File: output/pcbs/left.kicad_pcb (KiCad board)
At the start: 2 copper layers, 123.1 x 95.2 mm, 45 parts

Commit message: Position JST more robustly
also tuck thumbs up a little more
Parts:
- removed S19, S20, S21, S22, S23, S24, S25, S26, S27, S28, S29, S30, S31, S32, S33, S34, S35, S36: , ceoloide:switch_choc_v1_v2
- moved JST1 5.34 mm to (3.15, 18.9)
- moved H5 2.00 mm to (98.6, 1.56)
- moved S16 2.00 mm to (57.1, 7.18)
- moved S17 2.00 mm to (77.1, 9.48)
- moved S18 2.00 mm to (95.9, 16.3)
- moved H3 1.41 mm to (-5.60, 13.7)
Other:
- board size 123.1 x 95.2 mm -> 123.1 x 93.2 mm

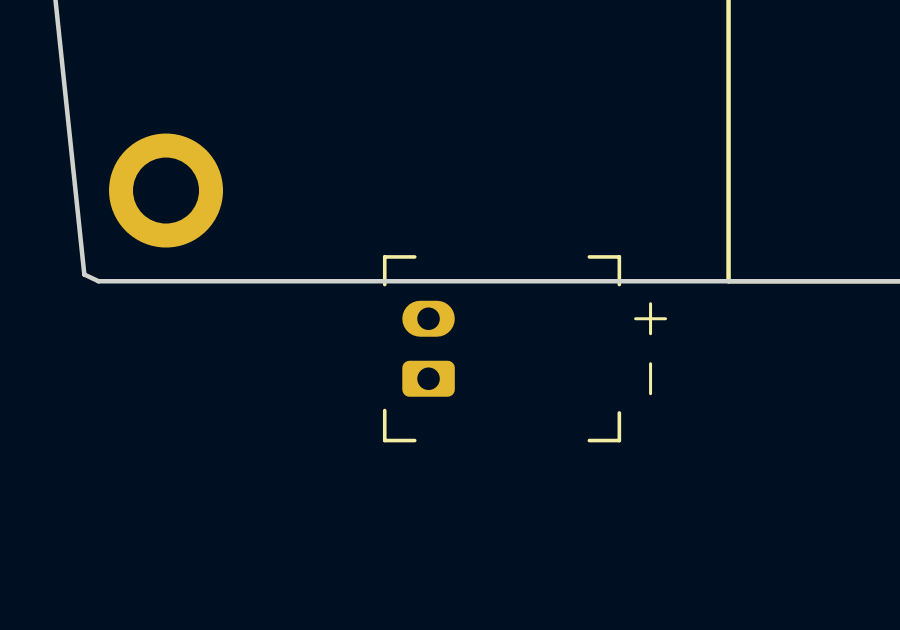
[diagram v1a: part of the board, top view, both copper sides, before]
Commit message: Make jst pcb and outline behave better
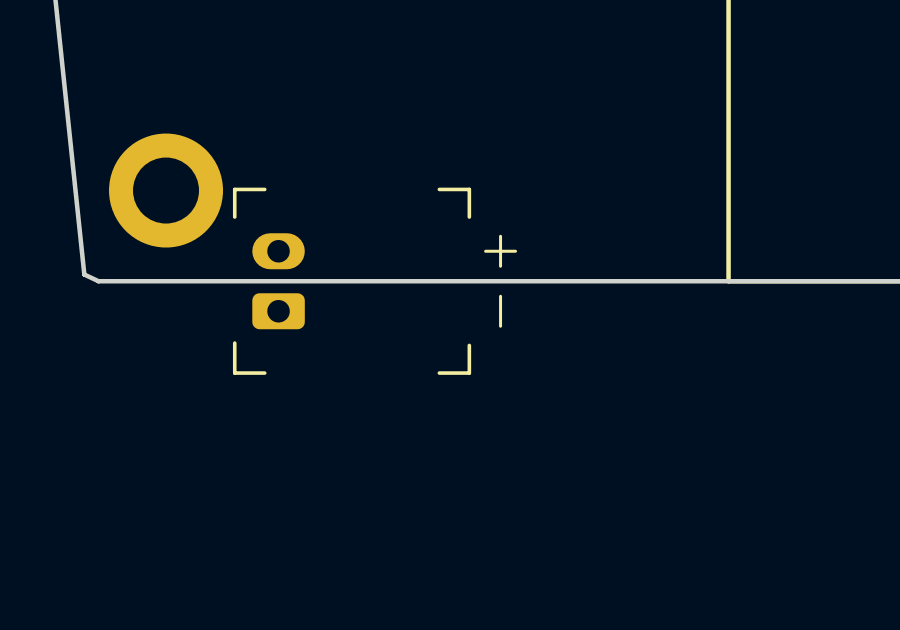
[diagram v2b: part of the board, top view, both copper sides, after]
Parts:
- moved JST1 5.48 mm to (-1.85, 16.7)
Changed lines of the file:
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@@
     (footprint "ceoloide:battery_connector_jst_ph_2"
         (layer "F.Cu")
-        (at 3.1483665999999957 18.9342912 90)
+        (at -1.8516334000000043 16.6842912 90)
         (property "Reference" "JST1"
             (at 0 4.8 90)

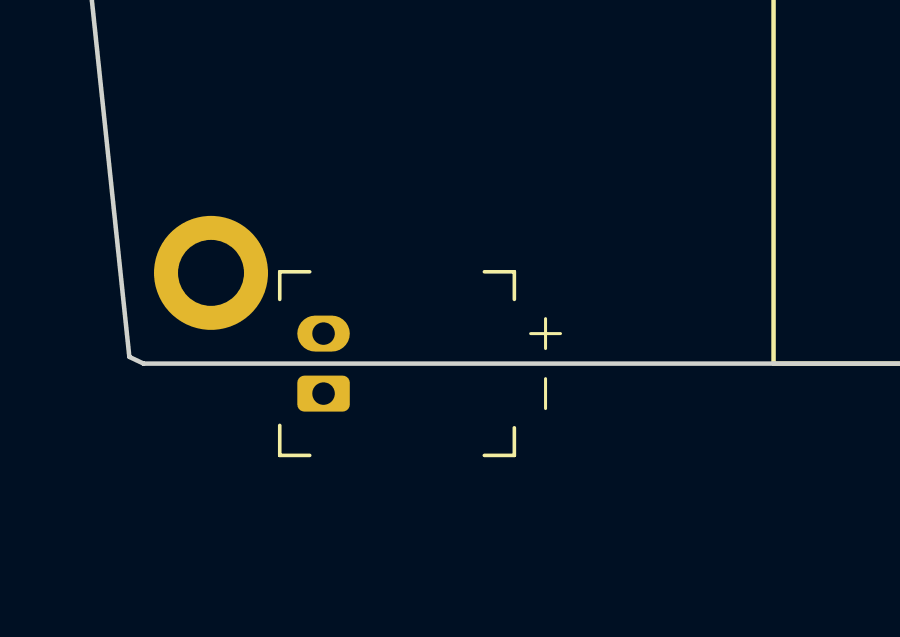
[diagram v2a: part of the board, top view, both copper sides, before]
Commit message: Tweaking jst outline+component
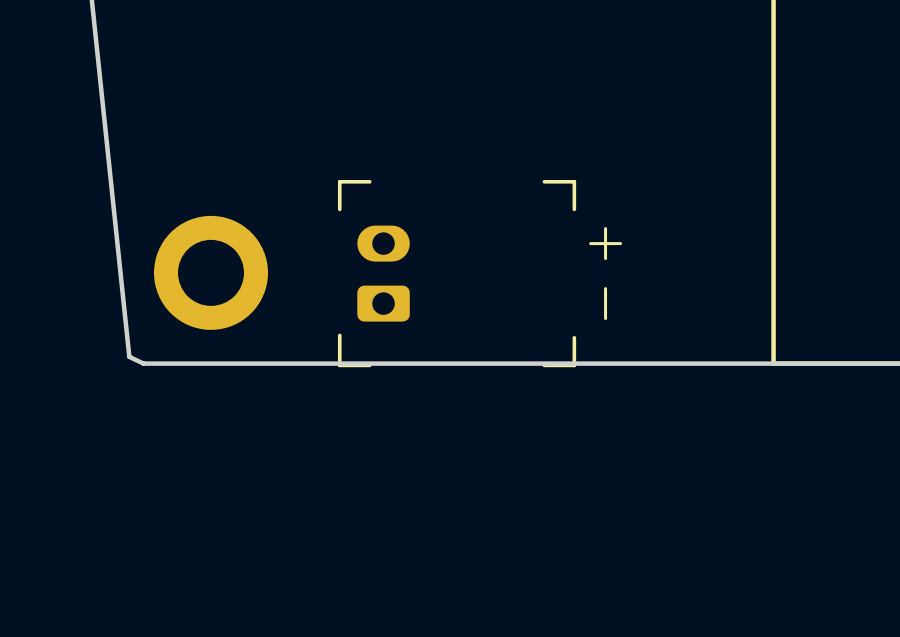
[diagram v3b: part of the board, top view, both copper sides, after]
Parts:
- moved JST1 3.61 mm to (0.15, 13.7)
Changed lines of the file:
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@@
     (footprint "ceoloide:battery_connector_jst_ph_2"
         (layer "F.Cu")
-        (at -1.8516334000000043 16.6842912 90)
+        (at 0.14836659999999569 13.6842912 90)
         (property "Reference" "JST1"
             (at 0 4.8 90)

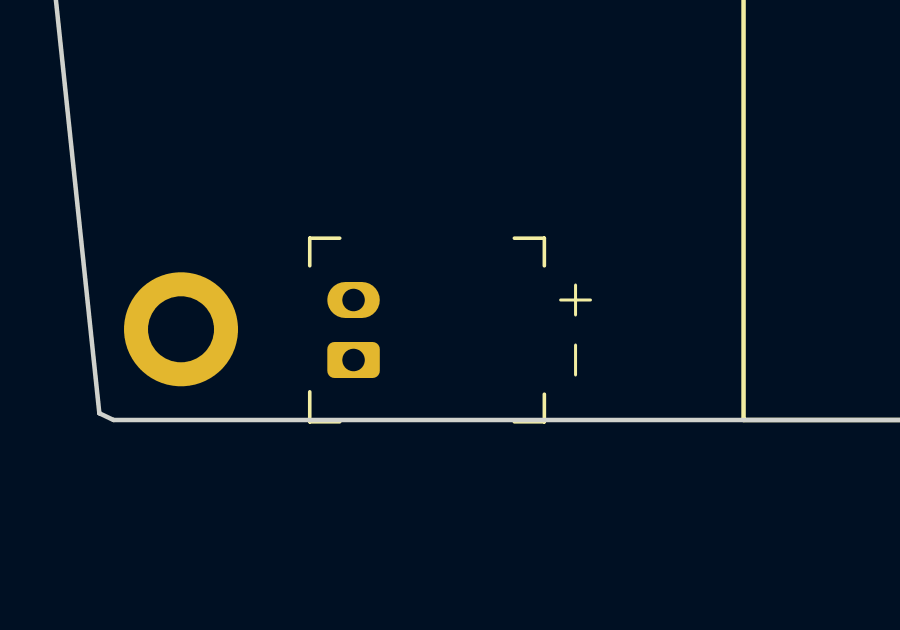
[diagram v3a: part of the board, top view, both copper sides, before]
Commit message: Nudge jst component up 1mm
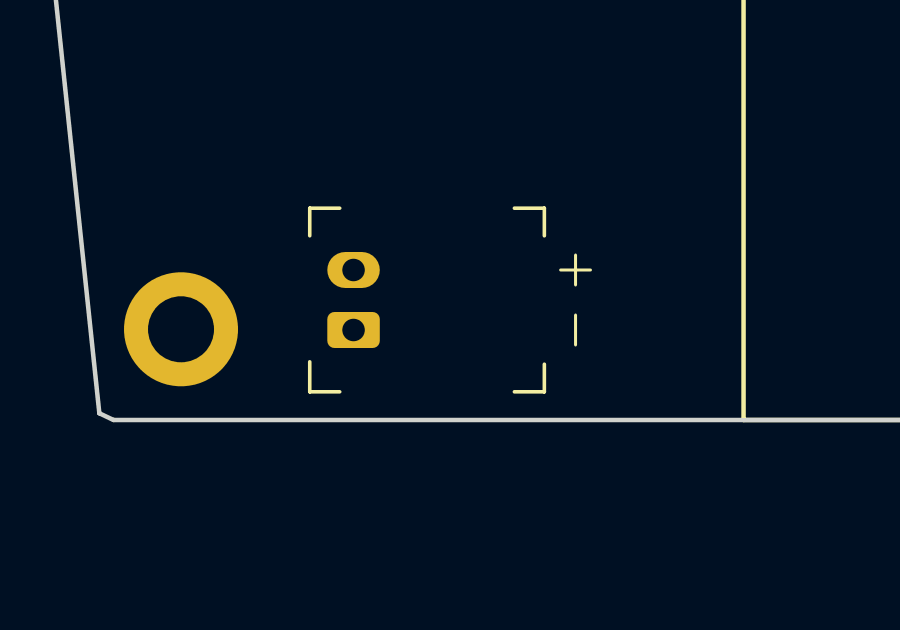
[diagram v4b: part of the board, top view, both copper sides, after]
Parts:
- moved JST1 1.00 mm to (0.15, 12.7)
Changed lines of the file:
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@@
     (footprint "ceoloide:battery_connector_jst_ph_2"
         (layer "F.Cu")
-        (at 0.14836659999999569 13.6842912 90)
+        (at 0.14836659999999569 12.6842912 90)
         (property "Reference" "JST1"
             (at 0 4.8 90)

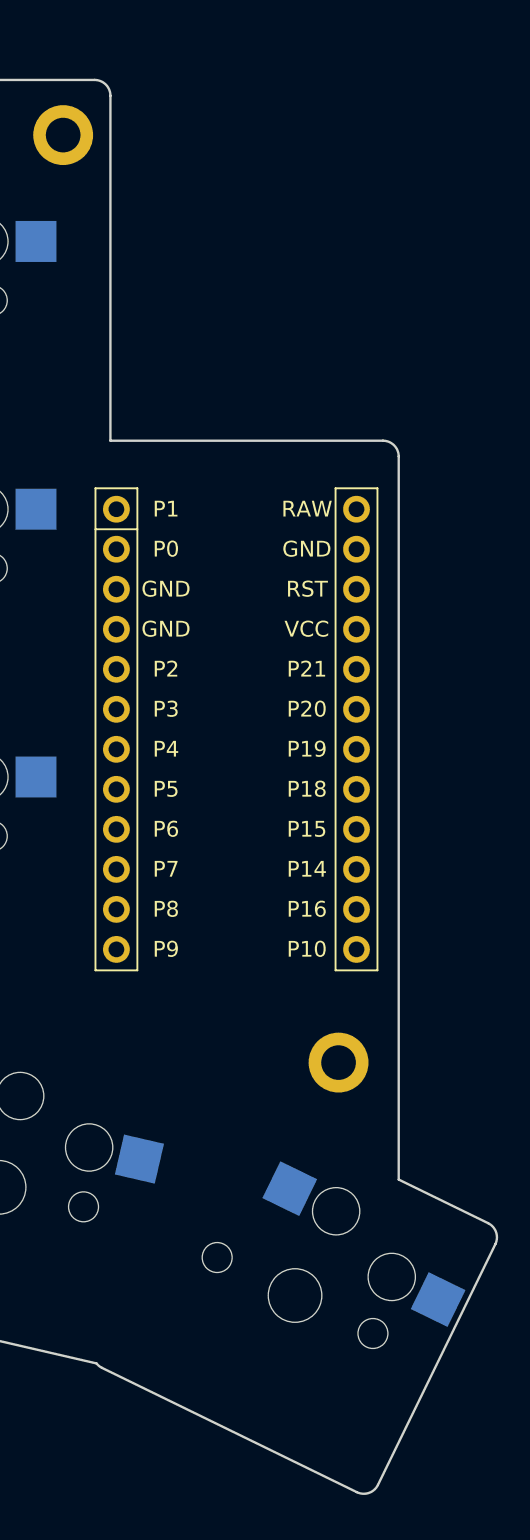
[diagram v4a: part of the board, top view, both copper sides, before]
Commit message: Try to share placement of controller outline + component
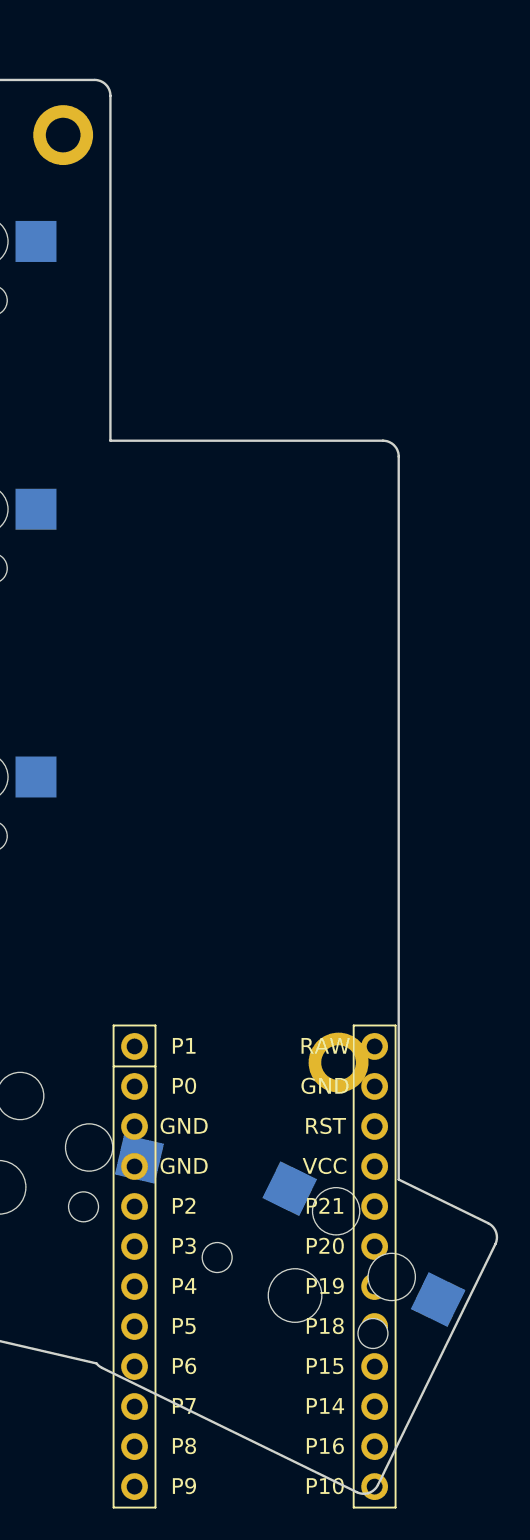
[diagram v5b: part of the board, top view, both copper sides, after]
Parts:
- moved MCU1 34.1 mm to (93.3, 13.2)
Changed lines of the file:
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@@
   (footprint "ceoloide:mcu_nice_nano"
     (layer "F.Cu")
-    (at 92.1483666 -20.8657089 0)
+    (at 93.29836660000001 13.2342911 0)
     (property "Reference" "MCU1"
       (at 0 -15 0)
@@
 (gr_line (start 101.13007150000001 28.368302800000002) (end 108.5819889 13.089608000000002) (layer Edge.Cuts) (stroke (width 0.15) (type default)))
 (gr_arc (start 108.582185 13.089205999999997) (mid 108.6289095 12.325266699999998) (end 108.1217621 11.752040899999997) (layer Edge.Cuts) (stroke (width 0.15) (type default)))
-(gr_line (start 108.1213601 11.751844899999998) (end 102.4483666 8.984941108545385) (layer Edge.Cuts) (stroke (width 0.15) (type default)))
+(gr_line (start 108.1213601 11.751844899999998) (end 102.44836660000001 8.984941108545392) (layer Edge.Cuts) (stroke (width 0.15) (type default)))
 (gr_line (start 24.54726792343898 -60.815708799999996) (end 25.148366699999997 -60.84721104908856) (layer Edge.Cuts) (stroke (width 0.15) (type default)))
-(gr_line (start 84.1483667 -37.9157089) (end 101.4483666 -37.9157089) (layer Edge.Cuts) (stroke (width 0.15) (type default)))
-(gr_line (start 102.4483666 8.984941108545385) (end 102.4483666 -36.9157089) (layer Edge.Cuts) (stroke (width 0.15) (type default)))
-(gr_arc (start 102.4483666 -36.9157089) (mid 102.1554734 -37.6228157) (end 101.4483666 -37.9157089) (layer Edge.Cuts) (stroke (width 0.15) (type default)))
+(gr_line (start 84.1483667 -37.915708900000006) (end 101.44836660000001 -37.915708900000006) (layer Edge.Cuts) (stroke (width 0.15) (type default)))
+(gr_line (start 102.44836660000001 8.984941108545392) (end 102.44836660000001 -36.9157089) (layer Edge.Cuts) (stroke (width 0.15) (type default)))
+(gr_arc (start 102.44836660000001 -36.9157089) (mid 102.15547340000002 -37.6228157) (end 101.44836660000001 -37.9157089) (layer Edge.Cuts) (stroke (width 0.15) (type default)))
 (gr_line (start -7.851633400000004 16.6842912) (end -8.3250278 16.460374) (layer Edge.Cuts) (stroke (width 0.15) (type default)))
 (gr_line (start -9.851633300000003 -42.7041617200161) (end -9.851633300000003 -59.815708799999996) (layer Edge.Cuts) (stroke (width 0.15) (type default)))
 (gr_line (start -8.851633300000003 -60.815708799999996) (end 24.54726792343898 -60.815708799999996) (layer Edge.Cuts) (stroke (width 0.15) (type default)))
 (gr_line (start 45.148366599999996 -60.815708799999996) (end 83.1483667 -60.815708799999996) (layer Edge.Cuts) (stroke (width 0.15) (type default)))
-(gr_line (start 84.1483667 -59.815708799999996) (end 84.1483667 -37.9157089) (layer Edge.Cuts) (stroke (width 0.15) (type default)))
+(gr_line (start 84.1483667 -59.815708799999996) (end 84.1483667 -37.915708900000006) (layer Edge.Cuts) (stroke (width 0.15) (type default)))
 (gr_arc (start -8.851633300000003 -60.815708799999996) (mid -9.558740100000003 -60.522815599999994) (end -9.851633300000003 -59.815708799999996) (layer Edge.Cuts) (stroke (width 0.15) (type default)))
 (gr_arc (start 84.1483667 -59.815708799999996) (mid 83.8554735 -60.522815599999994) (end 83.1483667 -60.815708799999996) (layer Edge.Cuts) (stroke (width 0.15) (type default)))

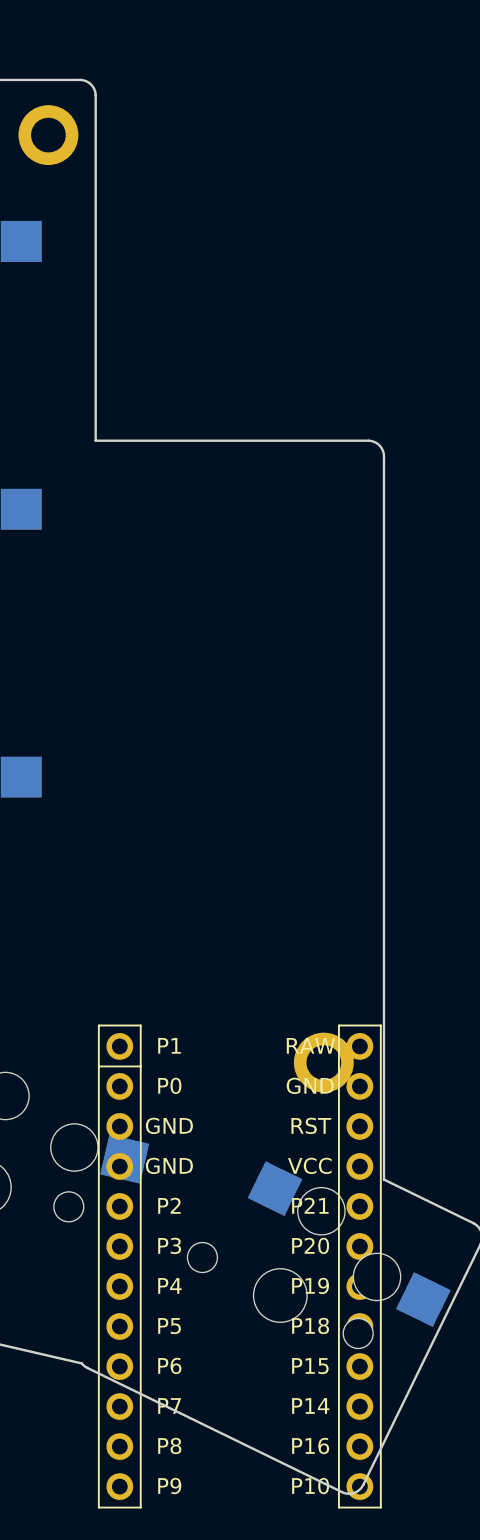
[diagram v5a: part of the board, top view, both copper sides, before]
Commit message: Fix bad math on controller outline
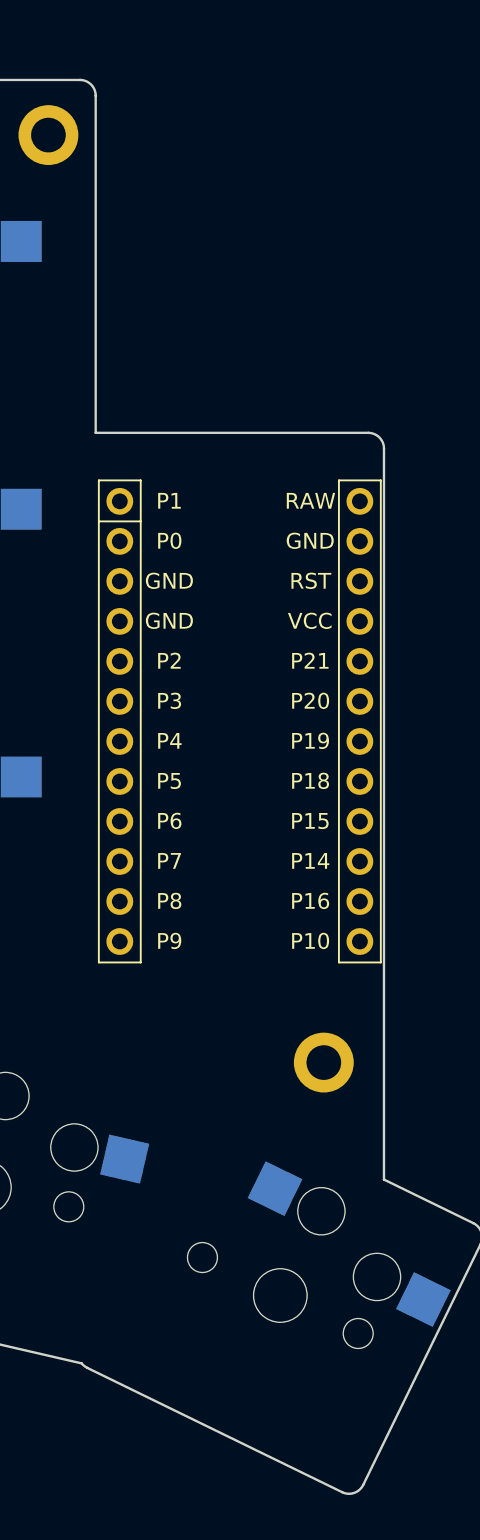
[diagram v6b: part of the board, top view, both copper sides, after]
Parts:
- moved MCU1 34.6 mm to (93.3, -21.4)
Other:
- outline, holes or cut-outs redrawn
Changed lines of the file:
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@@
   (footprint "ceoloide:mcu_nice_nano"
     (layer "F.Cu")
-    (at 93.29836660000001 13.2342911 0)
+    (at 93.29836660000001 -21.3657089 0)
     (property "Reference" "MCU1"
       (at 0 -15 0)
@@
 (gr_line (start 108.1213601 11.751844899999998) (end 102.44836660000001 8.984941108545392) (layer Edge.Cuts) (stroke (width 0.15) (type default)))
 (gr_line (start 24.54726792343898 -60.815708799999996) (end 25.148366699999997 -60.84721104908856) (layer Edge.Cuts) (stroke (width 0.15) (type default)))
-(gr_line (start 84.1483667 -37.915708900000006) (end 101.44836660000001 -37.915708900000006) (layer Edge.Cuts) (stroke (width 0.15) (type default)))
-(gr_line (start 102.44836660000001 8.984941108545392) (end 102.44836660000001 -36.9157089) (layer Edge.Cuts) (stroke (width 0.15) (type default)))
-(gr_arc (start 102.44836660000001 -36.9157089) (mid 102.15547340000002 -37.6228157) (end 101.44836660000001 -37.9157089) (layer Edge.Cuts) (stroke (width 0.15) (type default)))
+(gr_line (start 84.1483667 -38.4157089) (end 101.44836660000001 -38.4157089) (layer Edge.Cuts) (stroke (width 0.15) (type default)))
+(gr_line (start 102.44836660000001 8.984941108545392) (end 102.44836660000001 -37.4157089) (layer Edge.Cuts) (stroke (width 0.15) (type default)))
+(gr_arc (start 102.44836660000001 -37.4157089) (mid 102.15547340000002 -38.1228157) (end 101.44836660000001 -38.4157089) (layer Edge.Cuts) (stroke (width 0.15) (type default)))
 (gr_line (start -7.851633400000004 16.6842912) (end -8.3250278 16.460374) (layer Edge.Cuts) (stroke (width 0.15) (type default)))
 (gr_line (start -9.851633300000003 -42.7041617200161) (end -9.851633300000003 -59.815708799999996) (layer Edge.Cuts) (stroke (width 0.15) (type default)))
 (gr_line (start -8.851633300000003 -60.815708799999996) (end 24.54726792343898 -60.815708799999996) (layer Edge.Cuts) (stroke (width 0.15) (type default)))
 (gr_line (start 45.148366599999996 -60.815708799999996) (end 83.1483667 -60.815708799999996) (layer Edge.Cuts) (stroke (width 0.15) (type default)))
-(gr_line (start 84.1483667 -59.815708799999996) (end 84.1483667 -37.915708900000006) (layer Edge.Cuts) (stroke (width 0.15) (type default)))
+(gr_line (start 84.1483667 -59.815708799999996) (end 84.1483667 -38.4157089) (layer Edge.Cuts) (stroke (width 0.15) (type default)))
 (gr_arc (start -8.851633300000003 -60.815708799999996) (mid -9.558740100000003 -60.522815599999994) (end -9.851633300000003 -59.815708799999996) (layer Edge.Cuts) (stroke (width 0.15) (type default)))
 (gr_arc (start 84.1483667 -59.815708799999996) (mid 83.8554735 -60.522815599999994) (end 83.1483667 -60.815708799999996) (layer Edge.Cuts) (stroke (width 0.15) (type default)))
